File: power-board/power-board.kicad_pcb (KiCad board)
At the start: 4 copper layers, 90 x 70 mm, 133 parts, among them J1001 PA[5..7], J1002 PB[0..3], J1101 USB_OTG, J1102 CSHARE_IN, J1103 CSHARE_OUT, J301 CONN_01X02, J601 PDI, J801 CONN_02X05, J901 CONN_01X04, J902 CONN_01X04, J903 CONN_01X04, J904 CONN_01X04, J905 CONN_01X04, J906 PC[0..1], Q301 Q_NMOS_SSSGD, SW601 RESET, U1101 TPD2E001IDRLRQ1, U201 LMZ23610, U301 RT1720, U401 TLV521, U501 3.3v, U601 ATXMEGA32A4U-AU, U701 Main Reg, U901 CD4504B, Y601 16MHz

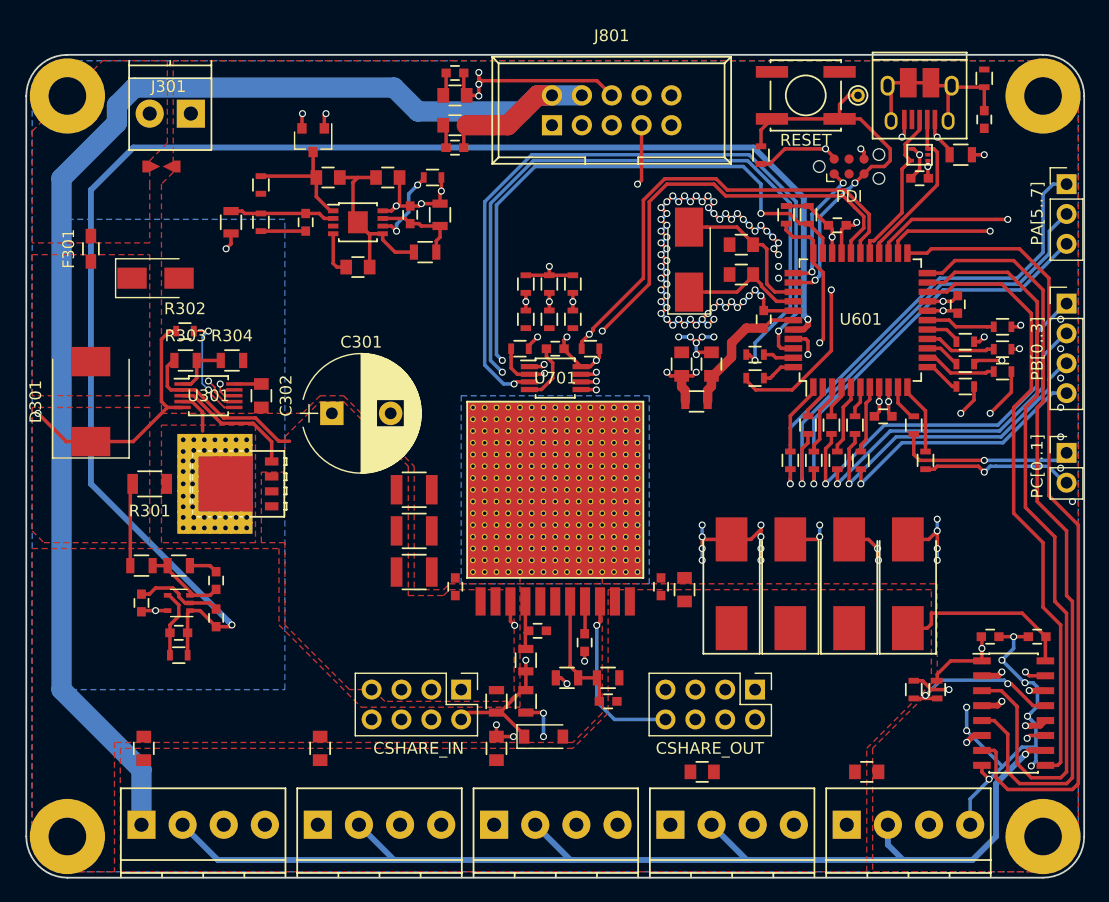
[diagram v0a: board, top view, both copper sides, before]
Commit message: cleaning up routing a bit, improving grounds, etc
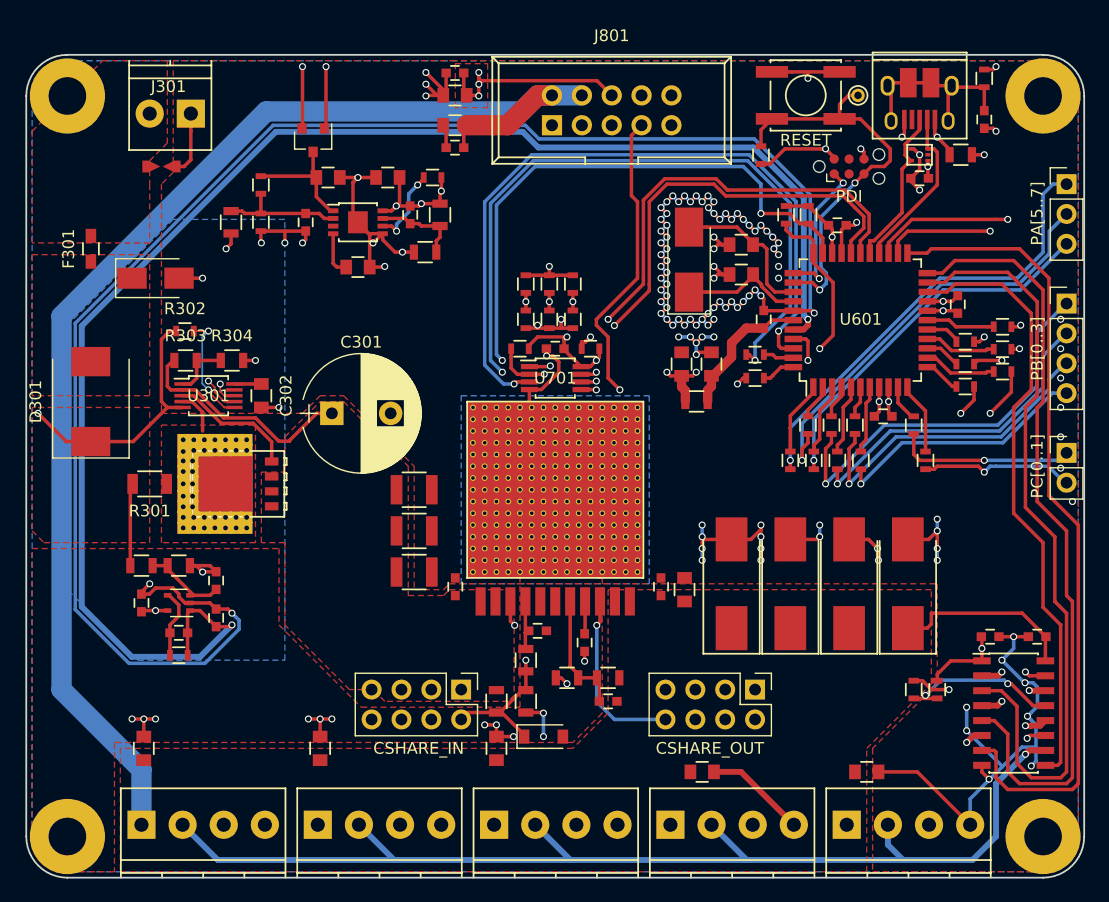
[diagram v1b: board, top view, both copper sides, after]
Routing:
- net GND: track 176.6 -> 477.0 mm, vias 105 -> 140
- net /Control Interface/5V_OUT: track 133.6 -> 124.2 mm
- net /Current Sharing/V_IN: track 14.8 -> 19.5 mm
- net /MCU/VBAT_SENSE: track 126.4 -> 130.6 mm
- net /Extra I/O/PA6: track 40.6 -> 36.6 mm
- net /Control Interface/SPI_INT: track 40.6 -> 36.7 mm
- net /Extra I/O/PA5: track 41.0 -> 38.5 mm
- net /Control Interface/3.3V_OUT: track 143.7 -> 146.2 mm, vias 18 -> 17
- net /Extra I/O/PA7: track 34.4 -> 31.9 mm
- net /Supervisor regulator/EN: track 8.95 -> 10.6 mm
- net /MCU/RESET: track 33.4 -> 35.0 mm
- net /MCU/PDI_DATA: track 11.4 -> 12.7 mm
- net /Current Sharing/ENABLE: track 65.4 -> 66.3 mm
- net /Power Entry/V_IN_UNFUSED: track 0.00 -> 0.76 mm
- net /MCU/SDA: track 45.9 -> 46.1 mm, vias 2 -> 3
- added copper zone on F.Cu, net /Control Interface/3.3V_OUT
